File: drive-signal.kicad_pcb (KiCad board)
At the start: 2 copper layers, 43.2 x 67.8 mm, 30 parts, among them J1 Conn_01x03_Pin, J10 Conn_01x04_Pin, J11 Conn_01x04_Pin, J2 Conn_01x03_Pin, J3 Conn_01x03_Pin, J4 Conn_01x03_Pin, J5 JETSON, J6 IMU, J7 Conn_01x02_Pin, J8 Conn_01x04_Pin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

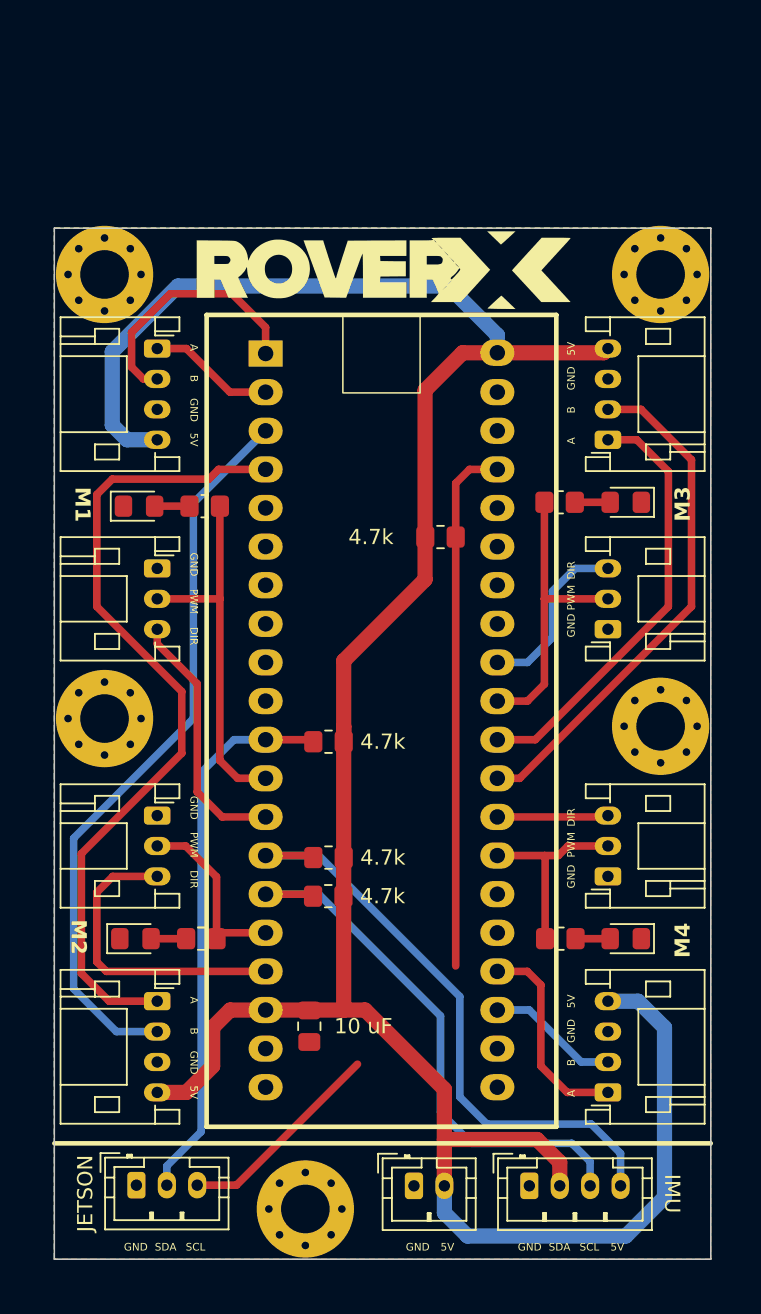
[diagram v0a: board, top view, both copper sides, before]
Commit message: reduce mounting holes
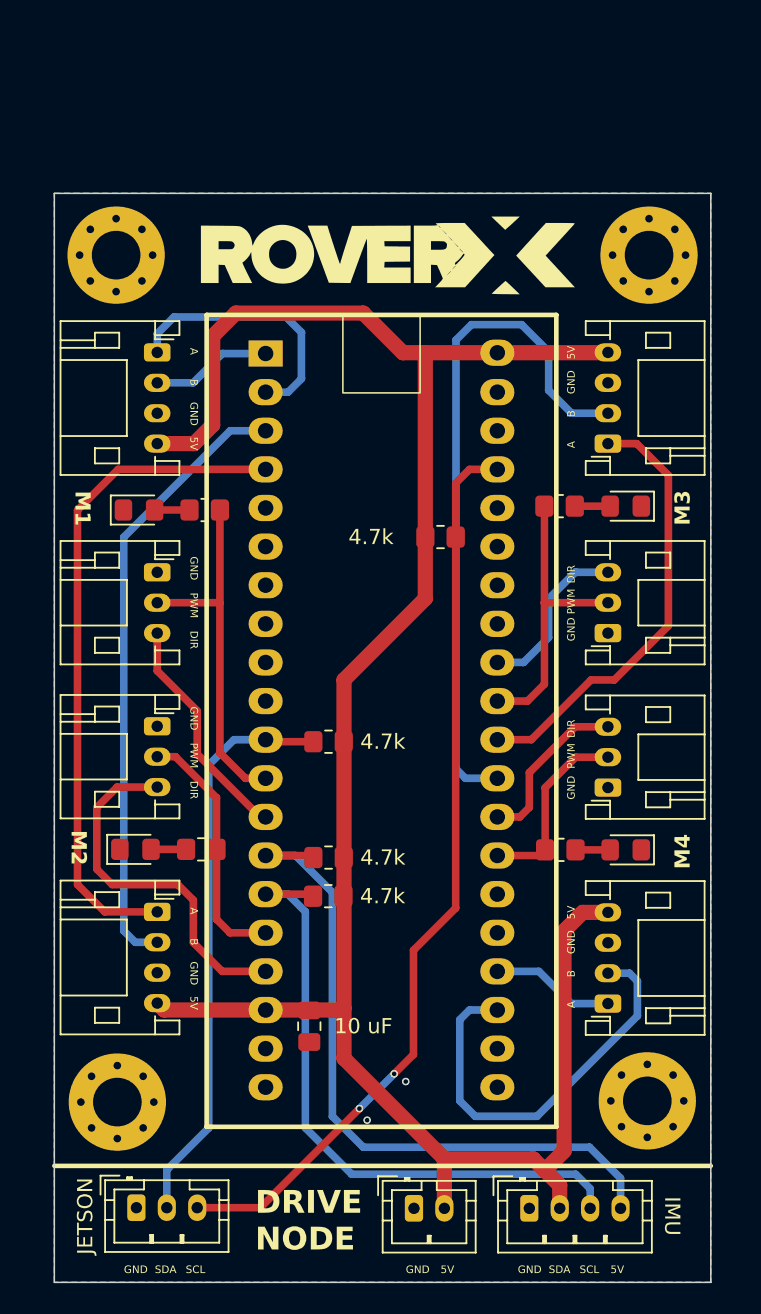
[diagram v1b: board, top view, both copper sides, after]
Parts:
- removed H5: MountingHole_Pad, MountingHole:MountingHole_3.2mm_M3_Pad_Via
- moved H3 25.2 mm to (50.9, 85.9)
- moved H4 24.7 mm to (85.7, 85.9)
- moved J9 5.87 mm to (53.5, 73.4)
- moved D1 5.87 mm to (52.1, 69.3)
- moved J2 5.87 mm to (53.5, 61.2)
- moved R5 5.87 mm to (56.4, 69.3)
- moved J10 5.84 mm to (83.1, 79.5)
- moved D3 5.84 mm to (84.3, 69.3)
- moved J3 5.84 mm to (83.1, 65.2)
- moved R7 5.84 mm to (80.0, 69.3)
- moved J5 1.48 mm to (52.1, 92.9)
- moved J6 1.48 mm to (78.0, 92.9)
- moved J7 1.48 mm to (70.4, 92.9)
- moved H1 1.48 mm to (85.9, 30.2)
- moved H2 1.48 mm to (50.8, 30.2)
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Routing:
- net +5V: track 169.4 -> 141.0 mm
- net RF_B: track 8.69 -> 27.4 mm
- net I2C2_J_SCL: track 48.7 -> 60.2 mm, vias 0 -> 2
- net RB_B: track 34.0 -> 45.5 mm
- net LB_A: track 54.1 -> 44.1 mm
- net LF_A: track 8.32 -> 17.4 mm
- net LF_B: track 16.8 -> 7.93 mm
- net LB_B: track 48.6 -> 40.6 mm
- net RF_A: track 13.7 -> 8.15 mm
- net I2C1_I_SCL: track 40.6 -> 45.9 mm
- net I2C1_I_SDA: track 37.1 -> 42.2 mm
- net PWM_LB: track 12.2 -> 16.6 mm
- net DIR_LB: track 20.3 -> 24.1 mm
- net DIR_RF: track 7.31 -> 11.1 mm
- net DIR_LF: track 17.0 -> 15.3 mm
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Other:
- board size 43.2 x 67.8 mm -> 43.2 x 71.6 mm
- board text added: "DRIVE NODE"

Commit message: done placement
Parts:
- added J12: IMU, Connector_PinHeader_2.54mm:PinHeader_1x08_P2.54mm_Vertical, F.Cu at (77.5, 89.4)
- added J13: I2C2 P1, Connector_JST:JST_EH_S3B-EH_1x03_P2.50mm_Horizontal, B.Cu at (59.7, 80.0)
- added J14: I2C2 P2, Connector_JST:JST_EH_S3B-EH_1x03_P2.50mm_Horizontal, B.Cu at (71.9, 80.0)
- J1, J2, J3, J4: footprint Connector_JST:JST_PH_S3B-PH-K_1x03_P2.00mm_Horizontal -> Connector_JST:JST_EH_S3B-EH_1x03_P2.50mm_Horizontal
- J10, J11, J8, J9: footprint Connector_JST:JST_PH_S4B-PH-K_1x04_P2.00mm_Horizontal -> Connector_JST:JST_EH_S4B-EH_1x04_P2.50mm_Horizontal
- J5: footprint Connector_JST:JST_PH_B3B-PH-K_1x03_P2.00mm_Vertical -> Connector_JST:JST_EH_B3B-EH-A_1x03_P2.50mm_Vertical
- J6: footprint Connector_JST:JST_PH_B4B-PH-K_1x04_P2.00mm_Vertical -> Connector_JST:JST_EH_B4B-EH-A_1x04_P2.50mm_Vertical
- J7: footprint Connector_JST:JST_PH_B2B-PH-K_1x02_P2.00mm_Vertical -> Connector_JST:JST_EH_B2B-EH-A_1x02_P2.50mm_Vertical
- moved J11 14.7 mm to (84.1, 28.0), turned to -90 degrees
- moved R4 13.5 mm to (72.1, 35.3)
- moved J4 10.4 mm to (84.1, 44.7), turned to -90 degrees
- moved H1 9.40 mm to (85.9, 20.8)
- moved H2 9.40 mm to (50.8, 20.8)
- moved R1 9.15 mm to (64.5, 63.2)
- moved R3 9.15 mm to (64.5, 53.1)
- moved R2 9.15 mm to (64.5, 60.7)
- moved U1 8.96 mm to (60.7, 27.8)
- moved C1 8.81 mm to (63.8, 72.1)
- moved J3 8.36 mm to (84.1, 56.9), turned to -90 degrees
- moved J10 8.33 mm to (84.1, 71.2), turned to -90 degrees
- moved D2 7.31 mm to (49.8, 40.1)
- moved R6 7.31 mm to (54.1, 40.1)
- moved R8 7.00 mm to (82.3, 40.1)
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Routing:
- net +5V: track 141.0 -> 0.00 mm
- net I2C2_J_SCL: track 60.2 -> 0.00 mm, vias 2 -> 0
- net I2C1_I_SCL: track 45.9 -> 0.00 mm
- net RB_B: track 45.5 -> 0.00 mm
- net LB_A: track 44.1 -> 0.00 mm
- net I2C1_I_SDA: track 42.2 -> 0.00 mm
- net LB_B: track 40.6 -> 0.00 mm
- net I2C2_J_SDA: track 37.9 -> 0.00 mm
- net RB_A: track 29.1 -> 0.00 mm
- net RF_B: track 27.4 -> 0.00 mm
- net DIR_LB: track 24.1 -> 0.00 mm
- net PWM_LF: track 23.8 -> 0.00 mm
- net PWM_RB: track 19.4 -> 0.00 mm
- net LF_A: track 17.4 -> 0.00 mm
- net PWM_LB: track 16.6 -> 0.00 mm
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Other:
- board size 43.2 x 71.6 mm -> 46 x 82.3 mm

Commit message: done something
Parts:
- moved J7 22.0 mm to (87.6, 85.1), turned to 180 degrees
- moved J6 15.0 mm to (64.6, 89.7)
- moved J13 12.2 mm to (71.9, 80.0)
- moved J14 12.2 mm to (59.7, 80.0)
- moved J5 9.13 mm to (49.1, 84.6)
- moved H3 5.92 mm to (50.7, 92.5)
- moved H4 5.92 mm to (85.6, 92.5)
- moved J12 5.85 mm to (77.2, 95.2)
- moved C1 0.25 mm to (63.8, 71.9)
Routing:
- net +5V: track 0.00 -> 175.0 mm
- net I2C2_J_SCL: track 0.00 -> 81.7 mm, vias 0 -> 1
- net I2C2_J_SDA: track 0.00 -> 71.0 mm, vias 0 -> 2
- net I2C1_I_SCL: track 0.00 -> 54.0 mm, vias 0 -> 2
- net I2C1_I_SDA: track 0.00 -> 51.2 mm, vias 0 -> 1
- net LB_B: track 0.00 -> 49.6 mm
- net LB_A: track 0.00 -> 49.2 mm
- net RB_B: track 0.00 -> 40.6 mm
- net PWM_LF: track 0.00 -> 32.0 mm
- net RB_A: track 0.00 -> 31.2 mm
- net PWM_RB: track 0.00 -> 29.8 mm
- net DIR_LB: track 0.00 -> 28.3 mm
- net PWM_RF: track 0.00 -> 20.4 mm
- net DIR_LF: track 0.00 -> 19.8 mm
- net PWM_LB: track 0.00 -> 15.8 mm
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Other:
- outline, holes or cut-outs redrawn
